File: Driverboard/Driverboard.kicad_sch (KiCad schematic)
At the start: 0 parts

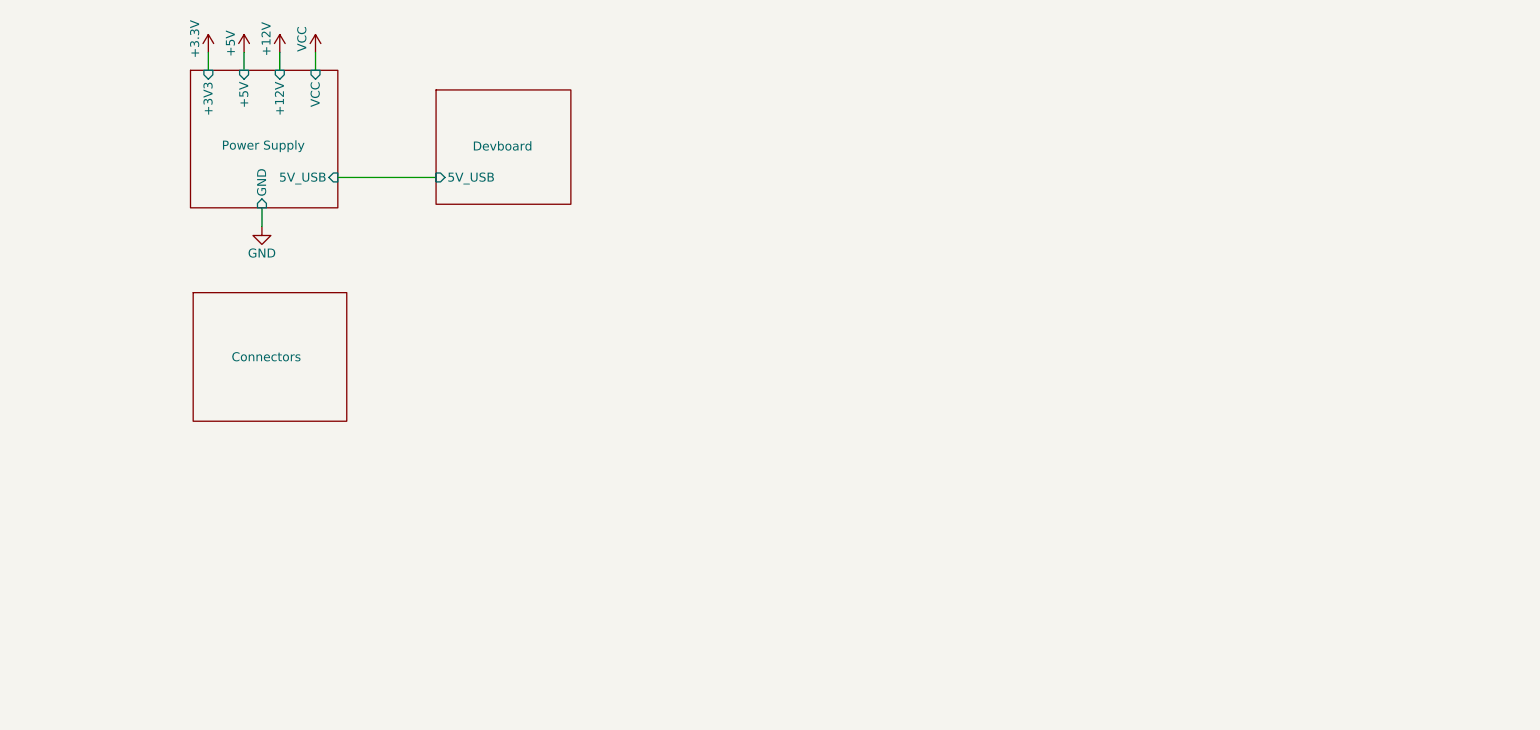
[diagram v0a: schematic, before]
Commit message: Motor Driver complete
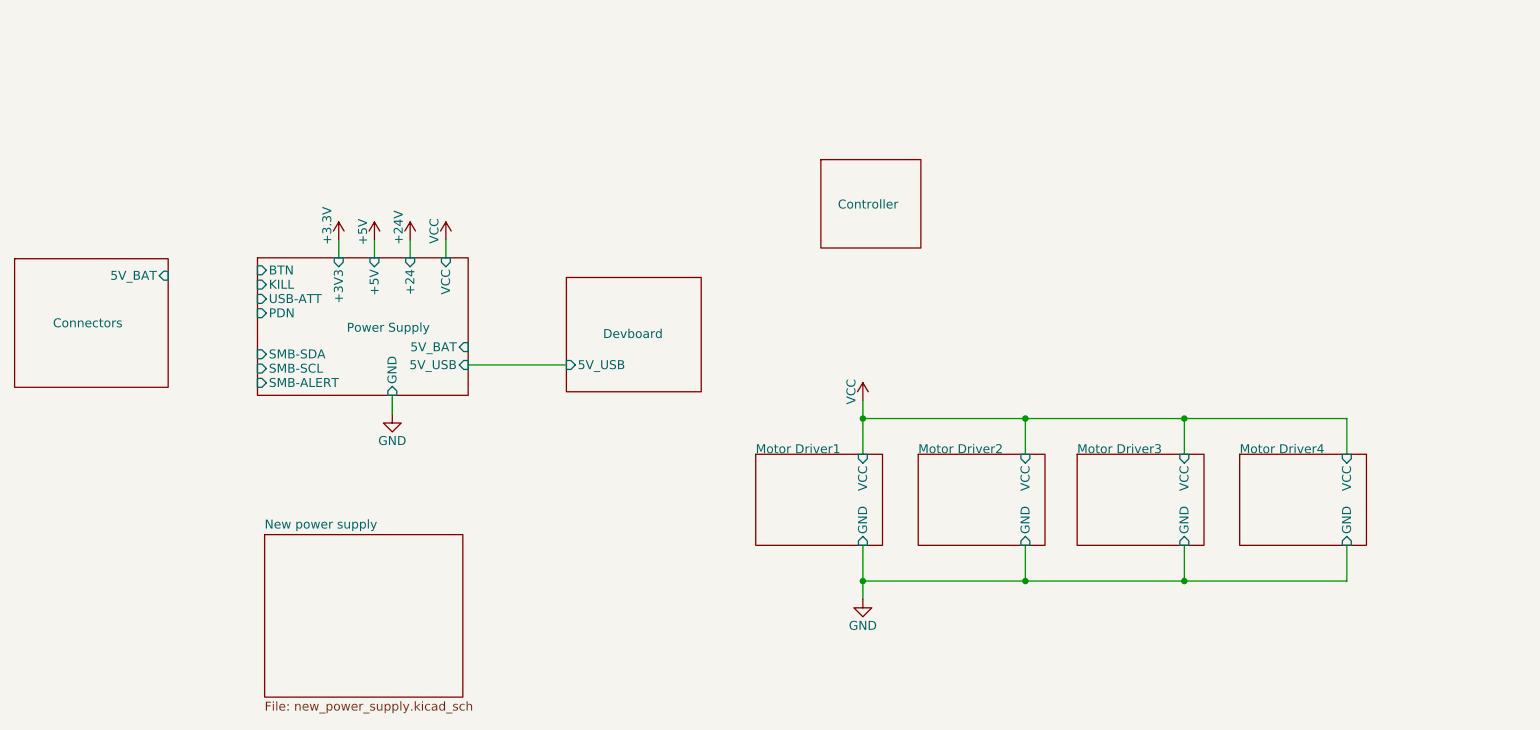
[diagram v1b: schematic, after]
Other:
- added sheet Controller (Controller.kicad_sch)
- added sheet Motor Driver1 (motor_driver.kicad_sch)
- added sheet Motor Driver2 (motor_driver.kicad_sch)
- added sheet Motor Driver3 (motor_driver.kicad_sch)
- added sheet Motor Driver4 (motor_driver.kicad_sch)
- added sheet New power supply (new_power_supply.kicad_sch)
- sheet Connectors ports: added 5V_BAT; removed none
- sheet Power Supply ports: added +24, 5V_BAT, BTN, KILL, PDN, SMB-ALERT, SMB-SCL, SMB-SDA, USB-ATT; removed +12V

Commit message: WIP
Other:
- added sheet Dribbler (motor_driver.kicad_sch)
